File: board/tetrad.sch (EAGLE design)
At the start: 89 parts, among them Q1 40V, U2 RADIO-ESP32_DEVKIT, U3 R-78E5.0-1.0

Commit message: started work on v1.1
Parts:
- Q1: value 40V -> FET-PCH-TO252
- Q10, Q11, Q12, Q2, Q3, Q4, Q5, Q6, Q7, Q8, Q9: value (none) -> FET-NCH-SOT23
- R1, R7: value 2k -> 1k
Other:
- note added: "40V"
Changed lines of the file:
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@@
 <part name="U2" library="holla" deviceset="RADIO-ESP32_DEVKIT" device=""/>
 <part name="U3" library="holla" deviceset="VREG" device="-SIP3" value="R-78E5.0-1.0"/>
-<part name="Q1" library="holla" deviceset="FET-PCH" device="-TO252" value="40V"/>
+<part name="Q1" library="holla" deviceset="FET-PCH" device="-TO252" value="FET-PCH-TO252"/>
 <part name="R17" library="holla" deviceset="R" device="-0603" value="100k"/>
 <part name="GND3" library="holla" deviceset="GND" device=""/>
@@
 <part name="GND16" library="holla" deviceset="GND" device=""/>
 <part name="R23" library="holla" deviceset="R" device="-0603" value="10k"/>
-<part name="R7" library="holla" deviceset="R" device="-0603" value="2k"/>
-<part name="R1" library="holla" deviceset="R" device="-0603" value="2k"/>
+<part name="R7" library="holla" deviceset="R" device="-0603" value="1k"/>
+<part name="R1" library="holla" deviceset="R" device="-0603" value="1k"/>
 <part name="GND17" library="holla" deviceset="GND" device=""/>
 <part name="GND18" library="holla" deviceset="GND" device=""/>
@@
 <text x="10.16" y="203.2" size="1.778" layer="97">todo
 add EVE2 display connector</text>
+<text x="36.83" y="157.48" size="1.016" layer="97">40V</text>
 </plain>
 <instances>

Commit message: updated schematic
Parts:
- U1: value (none) -> IO-MCP23017SO

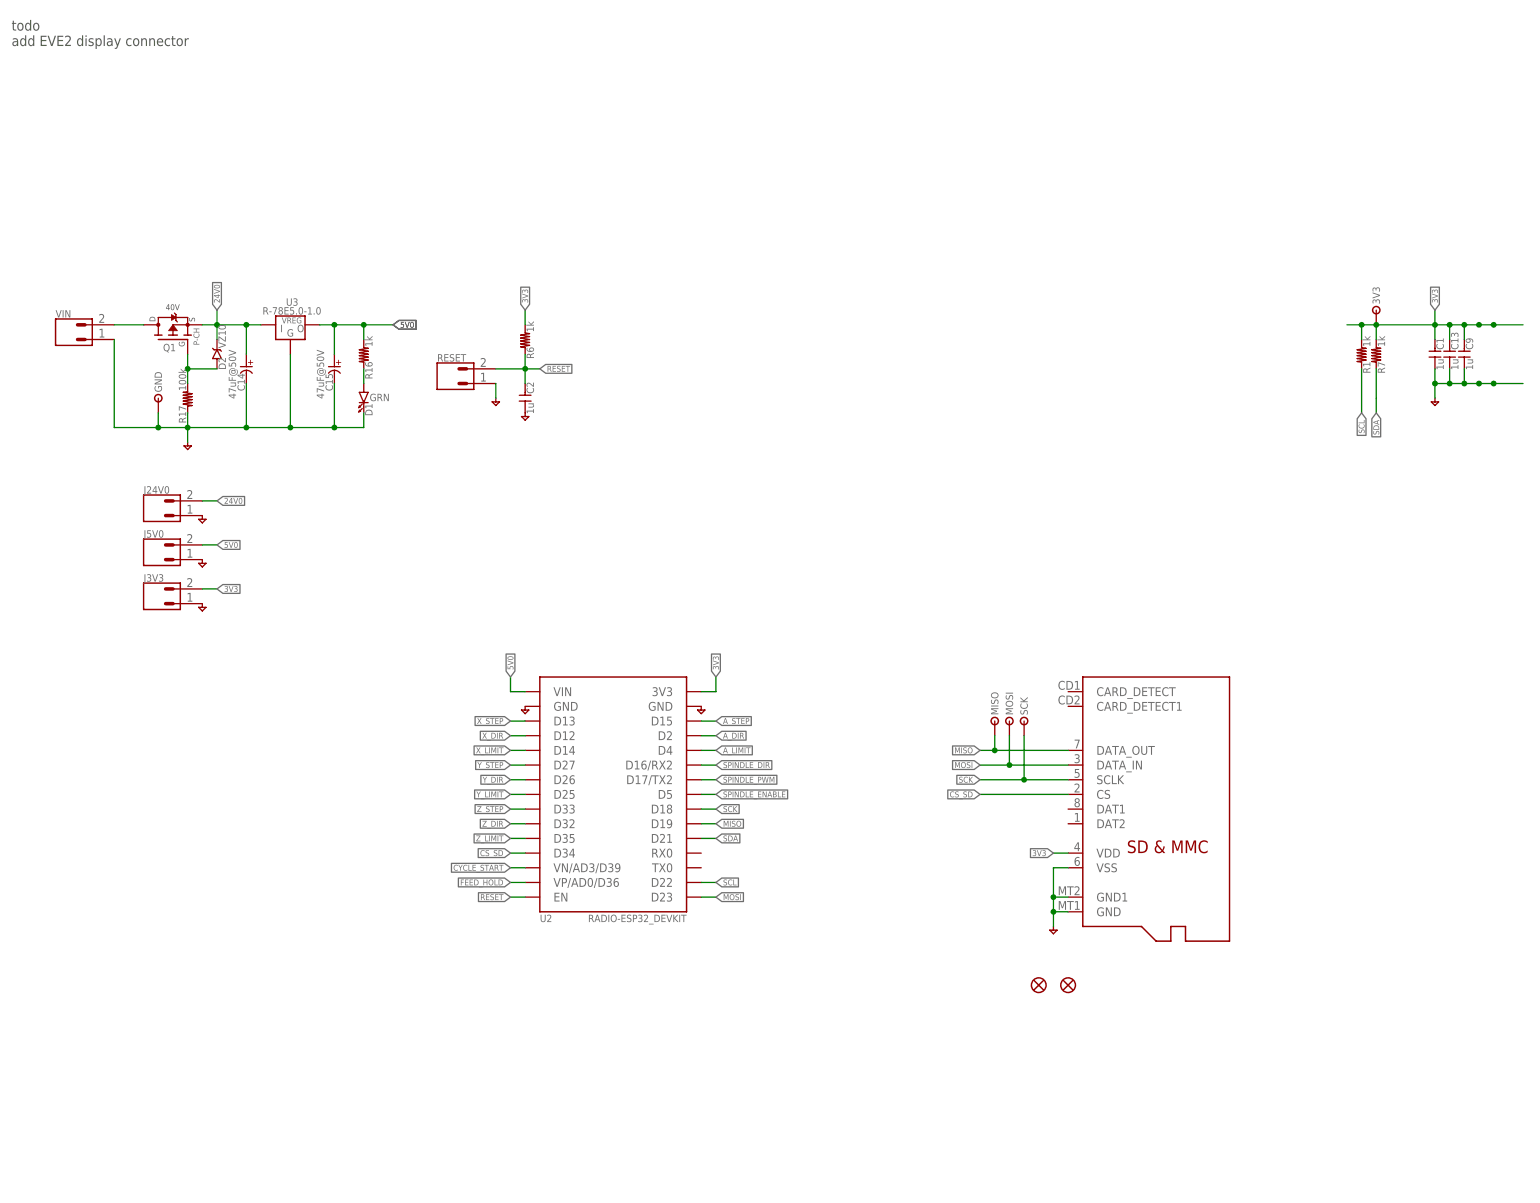
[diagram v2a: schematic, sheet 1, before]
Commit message: started fixing board mistakes
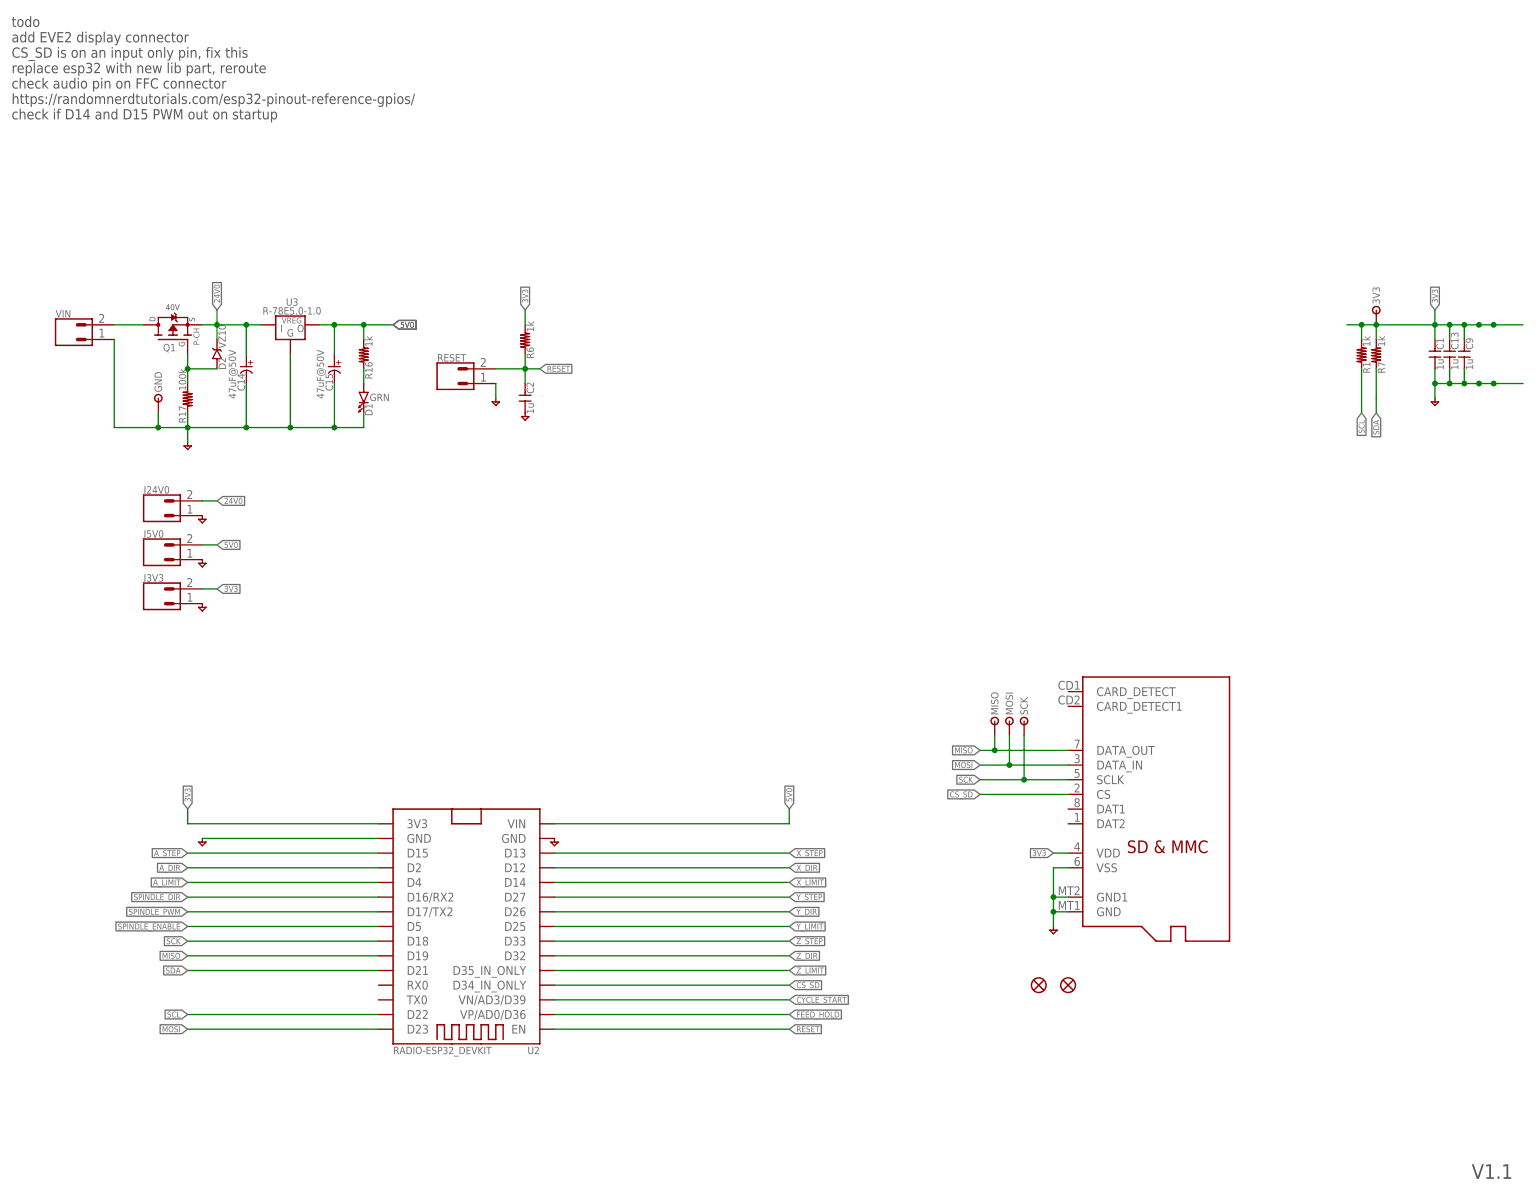
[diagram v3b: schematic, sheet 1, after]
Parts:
- added J17: (no value), holla:CONN-20-2-84952-0
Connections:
- new net AUDIO: J17.9
- new net CS_DISPLAY: J17.6
- new net INT_DISPLAY: J17.7
- new net PD_DISPLAY: J17.8
- net 3V3: now also J17.1, J17.17, J17.18
- net CS_SD: now also U2.D34_IN_ONLY; no longer U2.D34
- net GND: now also J17.19, J17.2, J17.20
- net MISO: now also J17.4
- net MOSI: now also J17.5
- net SCK: now also J17.3
- net Z_LIMIT: now also U2.D35_IN_ONLY; no longer U2.D35
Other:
- note added: "V1.1"
- note added: "todo add EVE2 display connector CS_SD is on an input only pin, fix this replace esp32 with new lib part, reroute check audio pin on FFC connector https://randomnerdtutorials.com/esp32-pinout-reference-gpios/ check if D14 and D15 PWM out on startup"
- note removed: "todo add EVE2 display connector"

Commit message: beefed up 24v0 traces
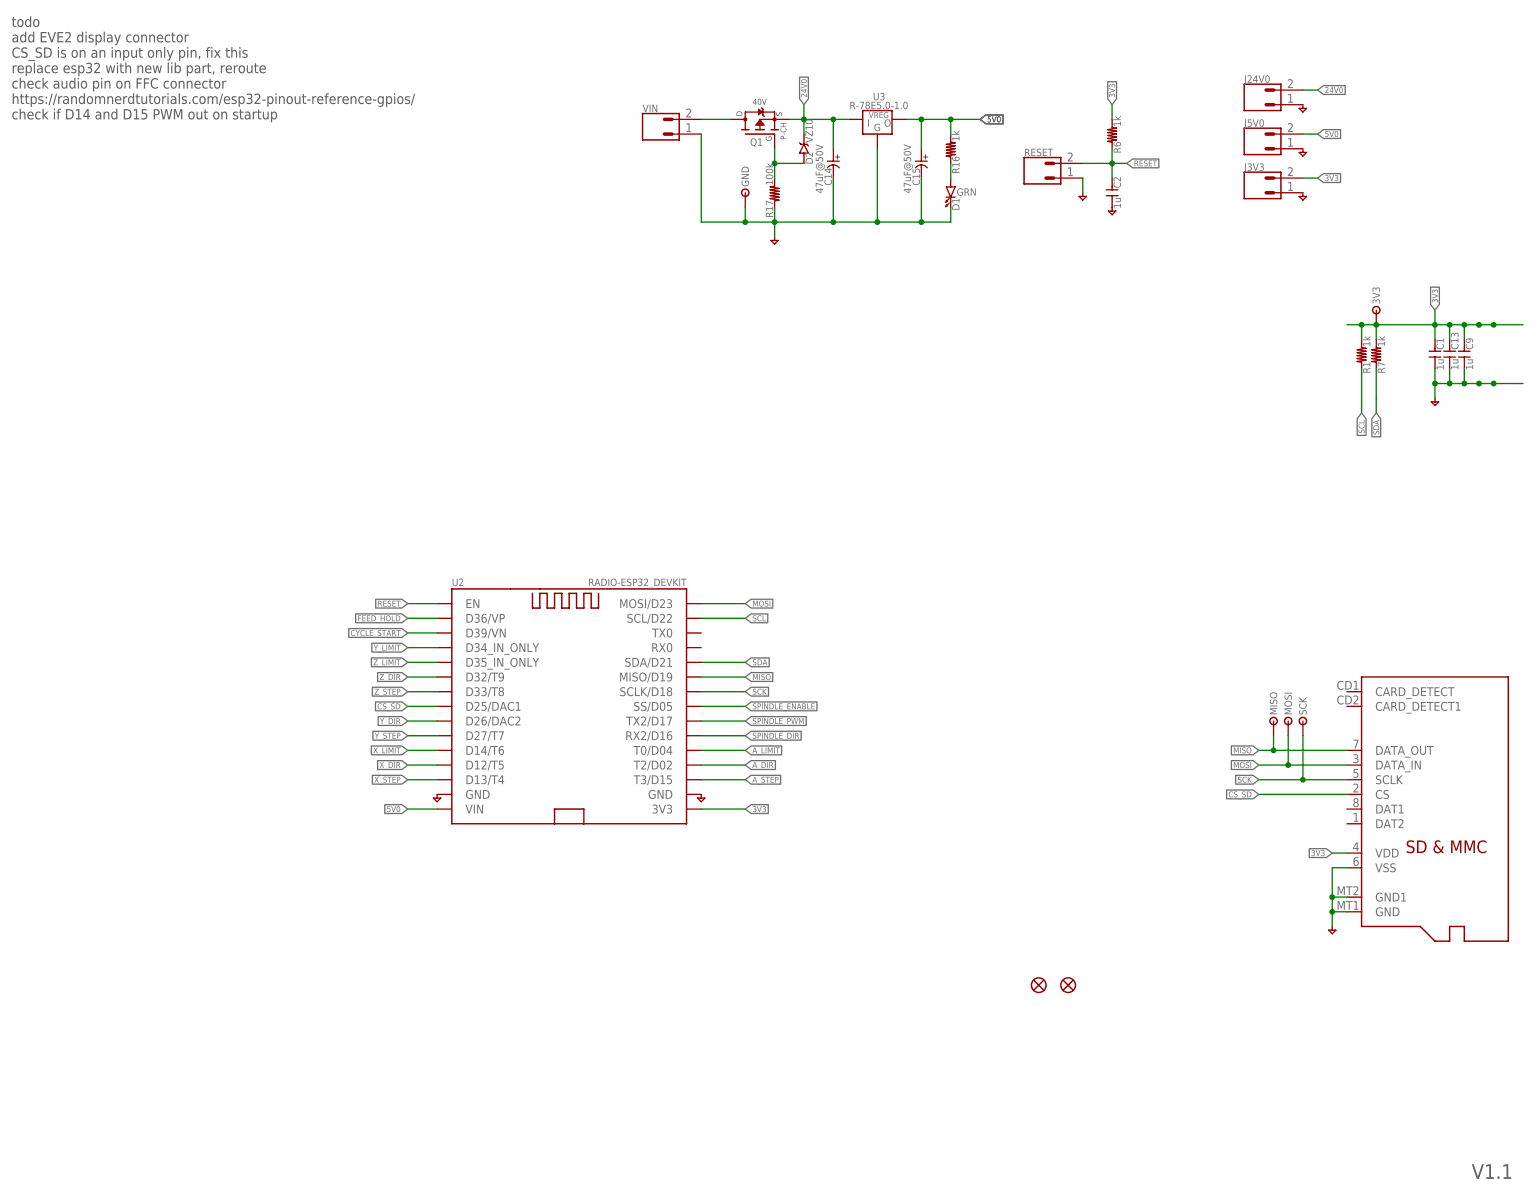
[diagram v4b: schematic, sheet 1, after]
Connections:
- net A_DIR: now also U2.T2/D02; no longer U2.D2
- net A_LIMIT: now also U2.T0/D04; no longer U2.D4
- net A_STEP: now also U2.T3/D15; no longer U2.D15
- net CS_SD: now also U2.D25/DAC1; no longer U2.D34_IN_ONLY
- net CYCLE_START: now also U2.D39/VN; no longer U2.VN/AD3/D39
- net FEED_HOLD: now also U2.D36/VP; no longer U2.VP/AD0/D36
- net MISO: now also U2.MISO/D19; no longer U2.D19
- net MOSI: now also U2.MOSI/D23; no longer U2.D23
- net SCK: now also U2.SCLK/D18; no longer U2.D18
- net SCL: now also U2.SCL/D22; no longer U2.D22
- net SDA: now also U2.SDA/D21; no longer U2.D21
- net SPINDLE_DIR: now also U2.RX2/D16; no longer U2.D16/RX2
- net SPINDLE_ENABLE: now also U2.SS/D05; no longer U2.D5
- net SPINDLE_PWM: now also U2.TX2/D17; no longer U2.D17/TX2
- net X_DIR: now also U2.D12/T5; no longer U2.D12
- net X_LIMIT: now also U2.D14/T6; no longer U2.D14
- net X_STEP: now also U2.D13/T4; no longer U2.D13
- net Y_DIR: now also U2.D26/DAC2; no longer U2.D26
- net Y_LIMIT: now also U2.D34_IN_ONLY; no longer U2.D25
- net Y_STEP: now also U2.D27/T7; no longer U2.D27
- net Z_DIR: now also U2.D32/T9; no longer U2.D32
- net Z_STEP: now also U2.D33/T8; no longer U2.D33
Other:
- moved on the sheet: C14, C15, C2, D1, D2, GND, J24V0, J3V3, J5V0, MISO, MOSI, Q1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

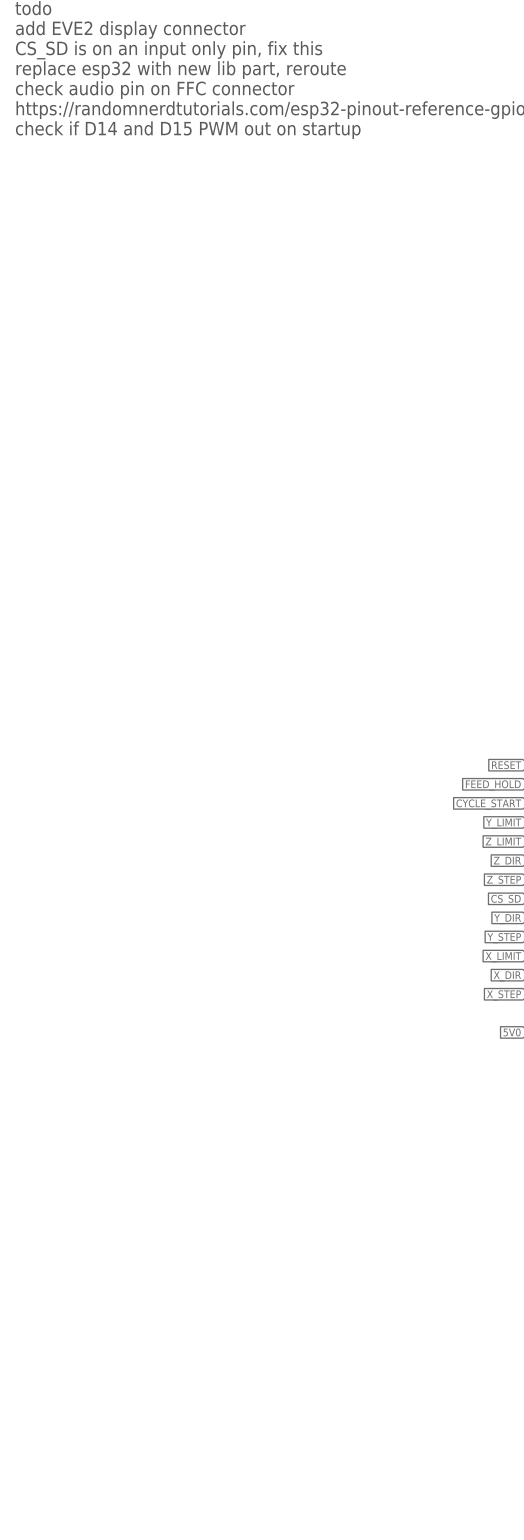
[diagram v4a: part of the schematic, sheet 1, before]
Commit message: starting add drv8825 slots and micro-fit connectors
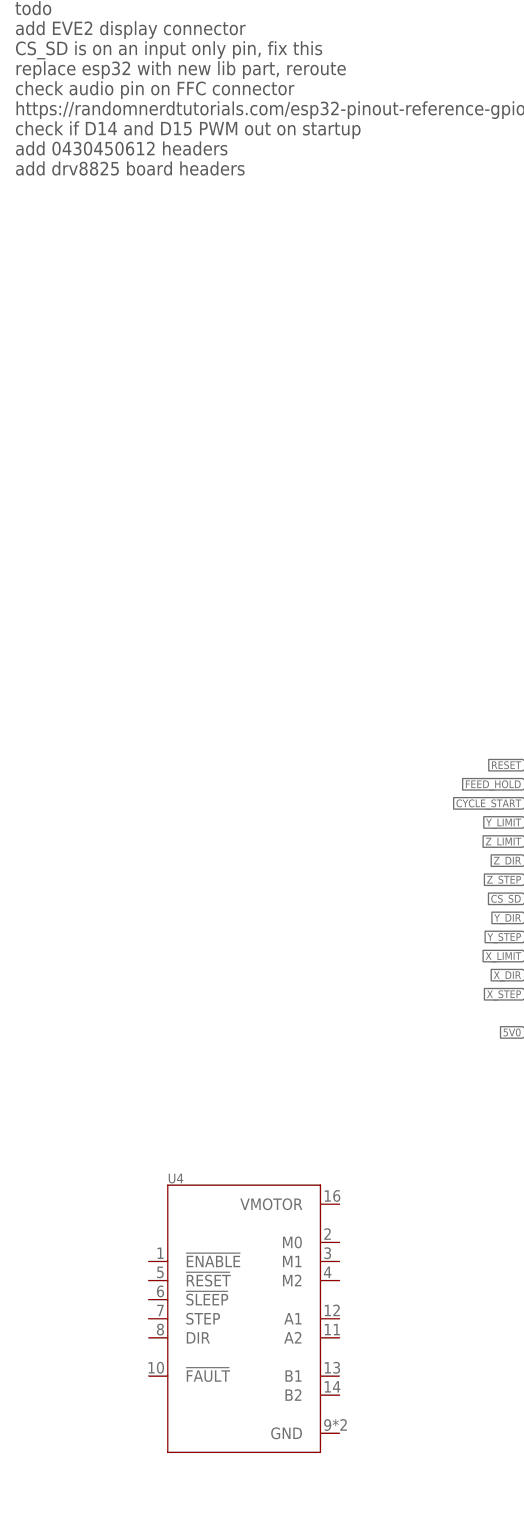
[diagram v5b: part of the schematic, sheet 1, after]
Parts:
- added J2: CONN-03X2-MICROFIT-430450612, holla:CONN-03X2-MICROFIT-430450612
- added U4: (no value), holla:BOARD-DRV8825-CARRIER
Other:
- note added: "todo add EVE2 display connector CS_SD is on an input only pin, fix this replace esp32 with new lib part, reroute check audio pin on FFC connector https://randomnerdtutorials.com/esp32-pinout-reference-gpios/ check if D14 and D15 PWM out on startup add 0430450612 headers add drv8825 board headers"
- note removed: "todo add EVE2 display connector CS_SD is on an input only pin, fix this replace esp32 with new lib part, reroute check audio pin on FFC connector https://randomnerdtutorials.com/esp32-pinout-reference-gpios/ check if D14 and D15 PWM out on startup"
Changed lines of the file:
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@@
 <part name="GND50" library="holla" deviceset="GND" device=""/>
 <part name="U2" library="holla" deviceset="RADIO-ESP32_DEVKIT" device=""/>
+<part name="J2" library="holla" deviceset="CONN-03X2-MICROFIT" device="-430450612"/>
+<part name="U4" library="holla" deviceset="BOARD-DRV8825-CARRIER" device=""/>
 </parts>
 <sheets>
@@
 check audio pin on FFC connector
 https://randomnerdtutorials.com/esp32-pinout-reference-gpios/
-check if D14 and D15 PWM out on startup</text>
+check if D14 and D15 PWM out on startup
+add 0430450612 headers
+add drv8825 board headers</text>
 <text x="138.43" y="193.04" size="1.016" layer="97">40V</text>
 <text x="262.89" y="7.112" size="2.54" layer="97">V1.1</text>
@@
 <instance part="RESET" gate="G$1" x="190.5" y="180.34"/>
 <instance part="U2" gate="G$1" x="106.68" y="88.9"/>
+<instance part="U4" gate="G$1" x="40.64" y="33.02"/>
 </instances>
 <busses>
@@
 <instance part="GND49" gate="1" x="203.2" y="142.24"/>
 <instance part="GND50" gate="1" x="203.2" y="93.98"/>
+<instance part="J2" gate="G$1" x="248.92" y="147.32"/>
 </instances>
 <busses>
